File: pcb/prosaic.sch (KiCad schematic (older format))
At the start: 16 parts, among them J1 USB_C_Receptacle, SW1 SW_PUSH, U1 ATMEGA32U4, X1 XTAL_GND

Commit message: Made moutning hole rearrangements
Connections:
- net col16: now reaches U1.36 (PF7)
- net col15: now reaches U1.37 (PF6)
- no-connect marks 18 -> 16
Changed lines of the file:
@@
 Sheet 1 2
 Title "Prosaic"
-Date "2020-07-18"
-Rev "-"
+Date "2020-07-28"
+Rev "A"
 Comp ""
-Comment1 "Keyboard, Controller"
-Comment2 ""
+Comment1 "by SiriusSam"
+Comment2 "Keyboard, Controller"
 Comment3 ""
 Comment4 ""
@@
 Text Label 1500 5200 0    50   ~ 0
 col4
+Text Label 1500 5350 0    50   ~ 0
+col5
 Text Label 3400 3850 0    50   ~ 0
-col5
+col6
 Text Label 3400 4000 0    50   ~ 0
-col6
+col7
 Text Label 3400 4150 0    50   ~ 0
-col7
+col8
 Text Label 3400 4300 0    50   ~ 0
-col8
+col9
 Text Label 3400 4450 0    50   ~ 0
-col9
+col10
 Text Label 3400 4600 0    50   ~ 0
-col10
+col11
 Text Label 3400 4750 0    50   ~ 0
-col11
+col12
 Text Label 3400 4900 0    50   ~ 0
-col12
+col13
 Text Label 3400 5050 0    50   ~ 0
-col13
-Text Label 3400 5200 0    50   ~ 0
 col14
 Wire Wire Line
@@
 	1500 5200 1750 5200
 Wire Wire Line
-	3250 3850 3400 3850
-Wire Wire Line
-	3400 4000 3250 4000
-Wire Wire Line
-	3250 4150 3400 4150
-Wire Wire Line
-	3400 4300 3250 4300
+	3400 3850 3250 3850
+Wire Wire Line
+	3250 4000 3400 4000
+Wire Wire Line
+	3400 4150 3250 4150
+Wire Wire Line
+	3250 4300 3400 4300
 Wire Wire Line
 	3250 4450 3400 4450
 Wire Wire Line
-	3250 4600 3400 4600
-Wire Wire Line
-	3400 4750 3250 4750
-Wire Wire Line
-	3250 4900 3400 4900
-Wire Wire Line
-	3400 5050 3250 5050
-Wire Wire Line
-	3250 5200 3400 5200
+	3400 4600 3250 4600
+Wire Wire Line
+	3250 4750 3400 4750
+Wire Wire Line
+	3400 4900 3250 4900
+Wire Wire Line
+	3250 5050 3400 5050
 Text Label 6400 4250 0    50   ~ 0
 row0
@@
 	8900 5450 8800 5450
 NoConn ~ 8800 3750
-NoConn ~ 8800 4250
-NoConn ~ 8800 4350
 NoConn ~ 8800 4750
 NoConn ~ 8800 4850
@@
 NoConn ~ 5500 3700
 $Sheet
-S 1750 3750 1500 1550
+S 1750 3750 1500 1700
 U 5F1B28AF
 F0 "Switch Matrix" 50
@@
 F10 "col3" I L 1750 5050 50
 F11 "col4" I L 1750 5200 50
-F12 "col5" I R 3250 3850 50
-F13 "col6" I R 3250 4000 50
-F14 "col7" I R 3250 4150 50
-F15 "col8" I R 3250 4300 50
-F16 "col9" I R 3250 4450 50
-F17 "col10" I R 3250 4600 50
-F18 "col11" I R 3250 4750 50
-F19 "col12" I R 3250 4900 50
-F20 "col13" I R 3250 5050 50
-F21 "col14" I R 3250 5200 50
+F12 "col5" I L 1750 5350 50
+F13 "col6" I R 3250 3850 50
+F14 "col7" I R 3250 4000 50
+F15 "col8" I R 3250 4150 50
+F16 "col9" I R 3250 4300 50
+F17 "col10" I R 3250 4450 50
+F18 "col11" I R 3250 4600 50
+F19 "col12" I R 3250 4750 50
+F20 "col13" I R 3250 4900 50
+F21 "col14" I R 3250 5050 50
+F22 "col15" I R 3250 5200 50
+F23 "col16" I R 3250 5350 50
 $EndSheet
+Wire Wire Line
+	1500 5350 1750 5350
+Text Label 3400 5200 0    50   ~ 0
+col15
+Text Label 3400 5350 0    50   ~ 0
+col16
+Wire Wire Line
+	3250 5200 3400 5200
+Wire Wire Line
+	3250 5350 3400 5350
+Text Label 8900 4250 0    50   ~ 0
+col15
+Text Label 8900 4350 0    50   ~ 0
+col16
+Wire Wire Line
+	8800 4250 8900 4250
+Wire Wire Line
+	8800 4350 8900 4350
 $EndSCHEMATC

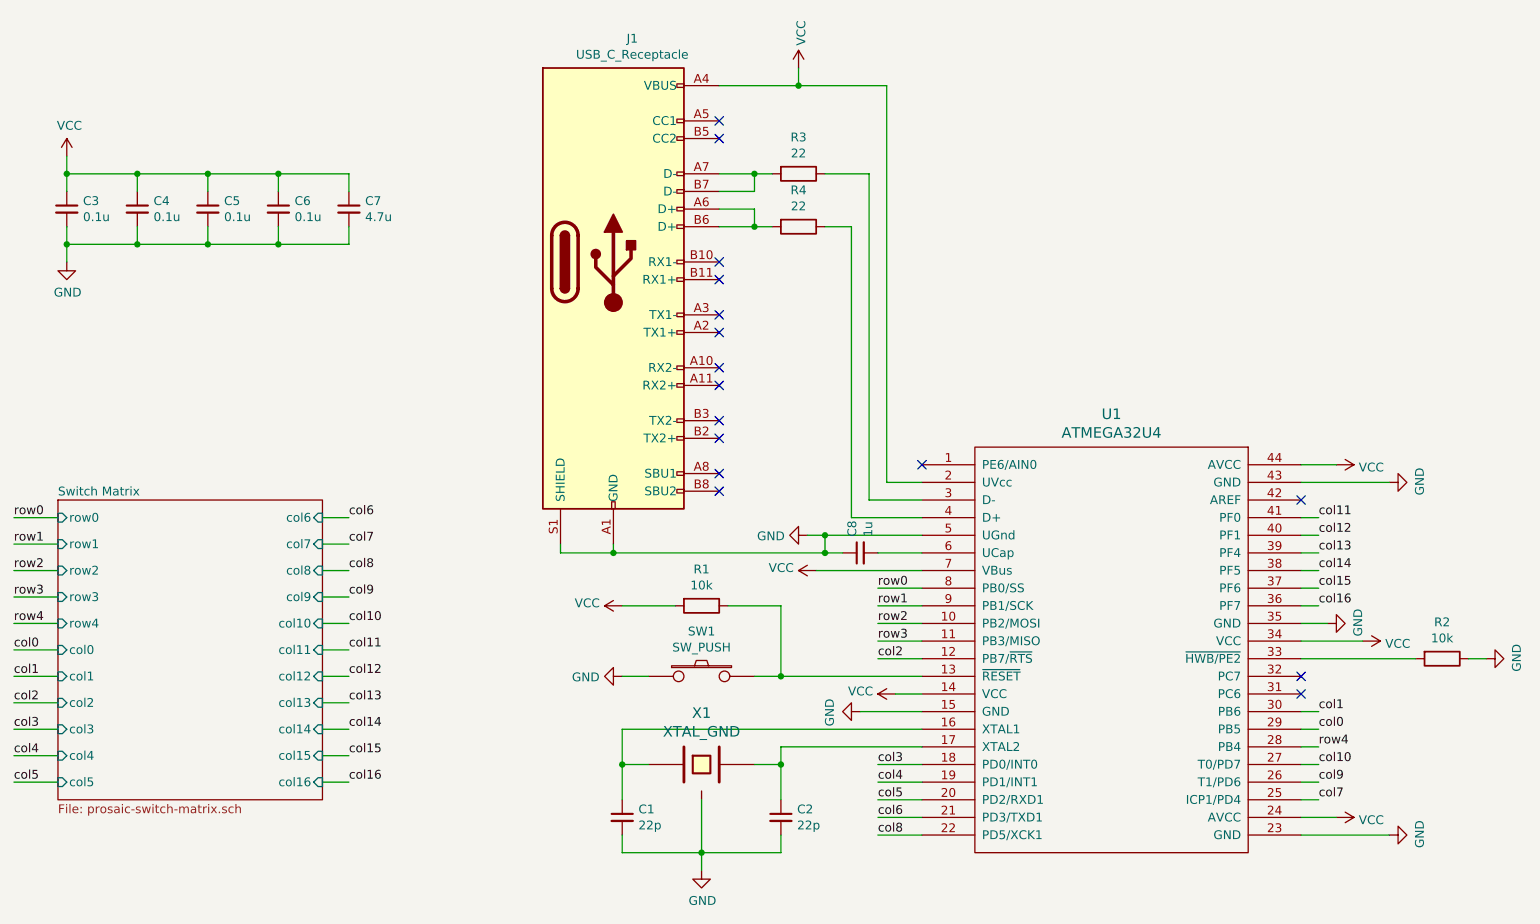
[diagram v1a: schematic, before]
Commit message: WIP: Ready for stabilizer verification
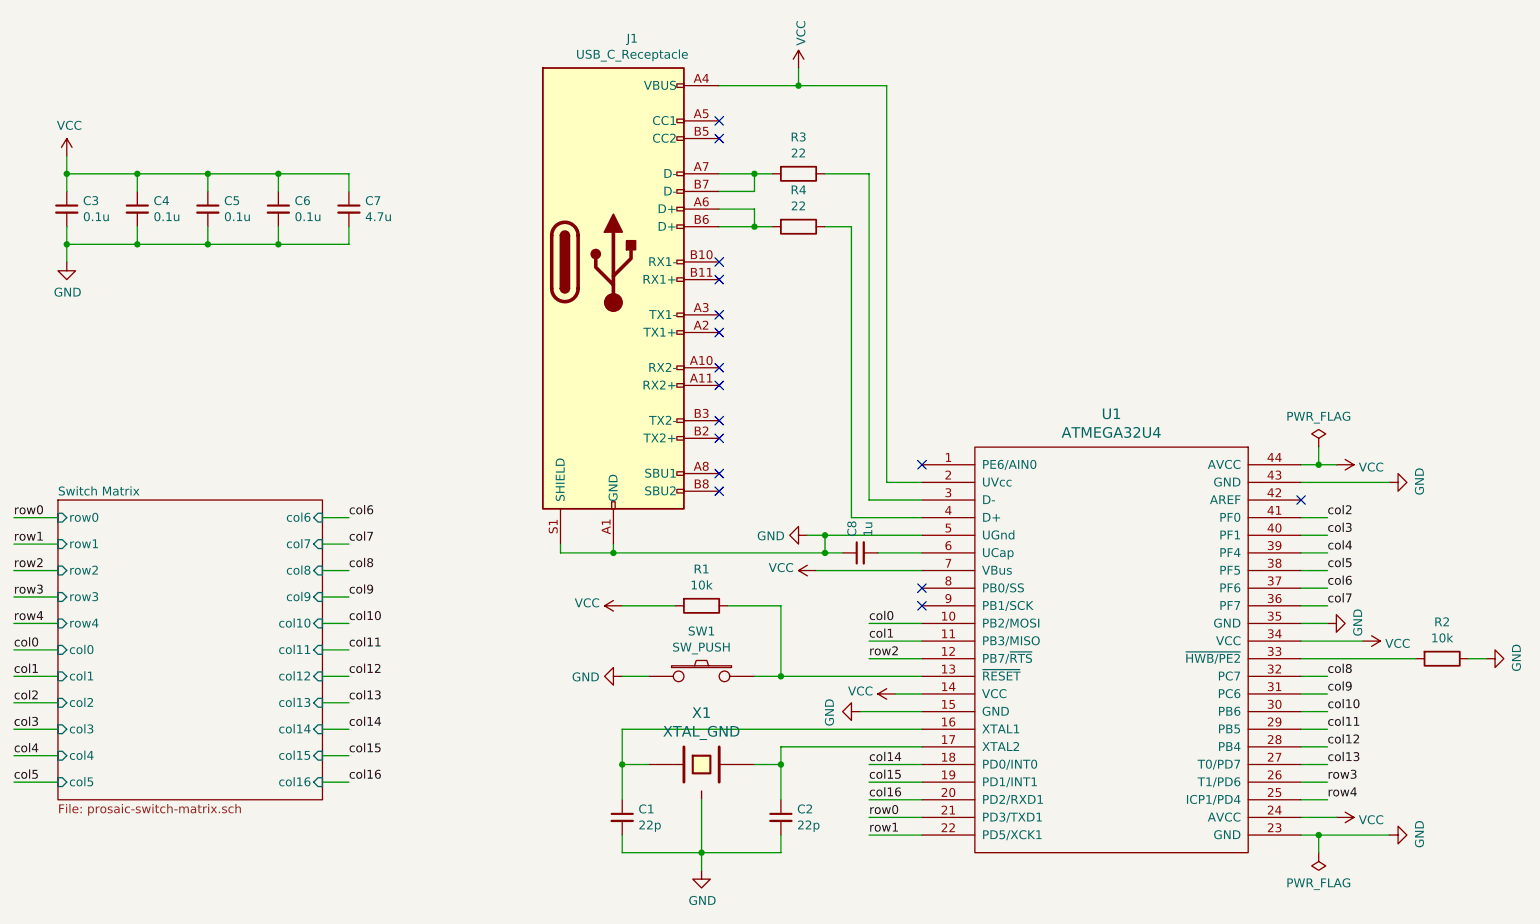
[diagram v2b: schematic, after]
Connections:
- net col0: now also U1.10 (PB2/MOSI); no longer U1.29 (PB5)
- net col1: now also U1.11 (PB3/MISO); no longer U1.30 (PB6)
- net col10: now also U1.30 (PB6); no longer U1.27 (T0/PD7)
- net col11: now also U1.29 (PB5); no longer U1.41 (PF0)
- net col12: now also U1.28 (PB4); no longer U1.40 (PF1)
- net col13: now also U1.27 (T0/PD7); no longer U1.39 (PF4)
- net col14: now also U1.18 (PD0/INT0); no longer U1.38 (PF5)
- net col15: now also U1.19 (PD1/INT1); no longer U1.37 (PF6)
- net col16: now also U1.20 (PD2/RXD1); no longer U1.36 (PF7)
- net col2: now also U1.41 (PF0); no longer U1.12 (PB7/~RTS)
- net col3: now also U1.40 (PF1); no longer U1.18 (PD0/INT0)
- net col4: now also U1.39 (PF4); no longer U1.19 (PD1/INT1)
- net col5: now also U1.38 (PF5); no longer U1.20 (PD2/RXD1)
- net col6: now also U1.37 (PF6); no longer U1.21 (PD3/TXD1)
- net col7: now also U1.36 (PF7); no longer U1.25 (ICP1/PD4)
- net col8: now also U1.32 (PC7); no longer U1.22 (PD5/XCK1)
- net col9: now also U1.31 (PC6); no longer U1.26 (T1/PD6)
- net row0: now also U1.21 (PD3/TXD1); no longer U1.8 (PB0/SS)
- net row1: now also U1.22 (PD5/XCK1); no longer U1.9 (PB1/SCK)
- net row2: now also U1.12 (PB7/~RTS); no longer U1.10 (PB2/MOSI)
- net row3: now also U1.26 (T1/PD6); no longer U1.11 (PB3/MISO)
- net row4: now also U1.25 (ICP1/PD4); no longer U1.28 (PB4)
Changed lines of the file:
@@
 Comment4 ""
 $EndDescr
-Wire Wire Line
-	6300 4950 6650 4950
 $Comp
 L power:GND #PWR0101
@@
 	0    1    1    0
 $EndComp
-Wire Wire Line
-	6500 4850 6650 4850
 $Comp
 L power:VCC #PWR0102
@@
 	0    -1   -1   0
 $EndComp
-Wire Wire Line
-	9000 5550 8800 5550
-Wire Wire Line
-	8800 5650 9300 5650
 $Comp
 L power:GND #PWR0104
@@
 	0    1    1    0
 $EndComp
-Wire Wire Line
-	8950 4450 8800 4450
 $Comp
 L power:GND #PWR0107
@@
 Wire Wire Line
 	8800 3650 9300 3650
-Wire Wire Line
-	8800 3550 9000 3550
 $Comp
 L power:GND #PWR0108
@@
 $EndComp
 Connection ~ 6100 4050
-Connection ~ 4900 4050
-Wire Wire Line
-	4900 4050 6100 4050
-Wire Wire Line
-	4600 4050 4900 4050
 Wire Wire Line
 	6100 3950 6650 3950
@@
 Text Label 1500 4750 0    50   ~ 0
 col1
-Text Label 1500 4900 0    50   ~ 0
-col2
 Text Label 1500 5050 0    50   ~ 0
 col3
@@
 	1750 4750 1500 4750
 Wire Wire Line
-	1500 4900 1750 4900
-Wire Wire Line
 	1750 5050 1500 5050
 Wire Wire Line
@@
 Wire Wire Line
 	3250 5050 3400 5050
-Text Label 6400 4250 0    50   ~ 0
-row0
-Text Label 6400 4350 0    50   ~ 0
-row1
-Text Label 6400 4450 0    50   ~ 0
-row2
-Text Label 6400 4550 0    50   ~ 0
-row3
-Text Label 8900 5150 0    50   ~ 0
-row4
-Text Label 8900 5050 0    50   ~ 0
-col0
-Text Label 8900 4950 0    50   ~ 0
-col1
-Text Label 6400 4650 0    50   ~ 0
-col2
-Text Label 6400 5250 0    50   ~ 0
-col3
-Text Label 6400 5350 0    50   ~ 0
-col4
-Text Label 6400 5450 0    50   ~ 0
-col5
-Text Label 6400 5550 0    50   ~ 0
-col6
-Text Label 8900 5450 0    50   ~ 0
-col7
-Text Label 6400 5650 0    50   ~ 0
-col8
-Text Label 8900 5350 0    50   ~ 0
-col9
-Text Label 8900 5250 0    50   ~ 0
-col10
-Text Label 8900 3850 0    50   ~ 0
-col11
-Text Label 8900 3950 0    50   ~ 0
-col12
-Text Label 8900 4050 0    50   ~ 0
-col13
-Text Label 8900 4150 0    50   ~ 0
-col14
-Wire Wire Line
-	6400 4250 6650 4250
-Wire Wire Line
-	6400 4350 6650 4350
-Wire Wire Line
-	6400 4450 6650 4450
-Wire Wire Line
-	6400 4550 6650 4550
-Wire Wire Line
-	6400 4650 6650 4650
-Wire Wire Line
-	6400 5250 6650 5250
-Wire Wire Line
-	6400 5350 6650 5350
-Wire Wire Line
-	6650 5450 6400 5450
-Wire Wire Line
-	6400 5550 6650 5550
-Wire Wire Line
-	6650 5650 6400 5650
-Wire Wire Line
-	8800 3850 8900 3850
-Wire Wire Line
-	8900 3950 8800 3950
-Wire Wire Line
-	8800 4050 8900 4050
-Wire Wire Line
-	8900 4150 8800 4150
-Wire Wire Line
-	8800 4950 8900 4950
-Wire Wire Line
-	8900 5050 8800 5050
-Wire Wire Line
-	8800 5150 8900 5150
-Wire Wire Line
-	8900 5250 8800 5250
-Wire Wire Line
-	8800 5350 8900 5350
-Wire Wire Line
-	8900 5450 8800 5450
 NoConn ~ 8800 3750
-NoConn ~ 8800 4750
-NoConn ~ 8800 4850
-NoConn ~ 6650 3550
 Wire Wire Line
 	6100 1900 6350 1900
@@
 Wire Wire Line
 	5950 1400 5500 1400
-Wire Wire Line
-	4900 4050 4900 4000
 $Comp
 L Connector:USB_C_Receptacle J1
@@
 F7 "col0" I L 1750 4600 50
 F8 "col1" I L 1750 4750 50
-F9 "col2" I L 1750 4900 50
-F10 "col3" I L 1750 5050 50
-F11 "col4" I L 1750 5200 50
-F12 "col5" I L 1750 5350 50
-F13 "col6" I R 3250 3850 50
-F14 "col7" I R 3250 4000 50
-F15 "col8" I R 3250 4150 50
-F16 "col9" I R 3250 4300 50
-F17 "col10" I R 3250 4450 50
-F18 "col11" I R 3250 4600 50
-F19 "col12" I R 3250 4750 50
-F20 "col13" I R 3250 4900 50
-F21 "col14" I R 3250 5050 50
-F22 "col15" I R 3250 5200 50
-F23 "col16" I R 3250 5350 50
+F9 "col3" I L 1750 5050 50
+F10 "col4" I L 1750 5200 50
+F11 "col5" I L 1750 5350 50
+F12 "col6" I R 3250 3850 50
+F13 "col7" I R 3250 4000 50
+F14 "col8" I R 3250 4150 50
+F15 "col9" I R 3250 4300 50
+F16 "col10" I R 3250 4450 50
+F17 "col11" I R 3250 4600 50
+F18 "col12" I R 3250 4750 50
+F19 "col13" I R 3250 4900 50
+F20 "col14" I R 3250 5050 50
+F21 "col15" I R 3250 5200 50
+F22 "col16" I R 3250 5350 50
+F23 "col2" I L 1750 4900 50
 $EndSheet
 Wire Wire Line
@@
 Wire Wire Line
 	3250 5350 3400 5350
-Text Label 8900 4250 0    50   ~ 0
+Text Label 6350 5250 0    50   ~ 0
+col14
+Text Label 6350 5350 0    50   ~ 0
 col15
-Text Label 8900 4350 0    50   ~ 0
+Text Label 6350 5450 0    50   ~ 0
 col16
-Wire Wire Line
-	8800 4250 8900 4250
-Wire Wire Line
-	8800 4350 8900 4350
+Text Label 6350 5550 0    50   ~ 0
+row0
+Text Label 6350 5650 0    50   ~ 0
+row1
+Wire Wire Line
+	6350 5250 6650 5250
+Wire Wire Line
+	6650 5350 6350 5350
+Wire Wire Line
+	6350 5450 6650 5450
+Wire Wire Line
+	6650 5550 6350 5550
+Wire Wire Line
+	6350 5650 6650 5650
+Text Label 8950 5450 0    50   ~ 0
+row4
+Text Label 8950 5350 0    50   ~ 0
+row3
+Text Label 6350 4650 0    50   ~ 0
+row2
+Text Label 8950 5250 0    50   ~ 0
+col13
+Text Label 8950 5150 0    50   ~ 0
+col12
+Text Label 8950 5050 0    50   ~ 0
+col11
+Text Label 8950 4950 0    50   ~ 0
+col10
+Text Label 8950 4850 0    50   ~ 0
+col9
+Text Label 8950 4750 0    50   ~ 0
+col8
+Text Label 8950 4350 0    50   ~ 0
+col7
+Text Label 8950 4250 0    50   ~ 0
+col6
+Text Label 8950 4150 0    50   ~ 0
+col5
+Text Label 8950 4050 0    50   ~ 0
+col4
+Text Label 8950 3950 0    50   ~ 0
+col3
+Text Label 6350 4550 0    50   ~ 0
+col1
+Text Label 6350 4450 0    50   ~ 0
+col0
+Wire Wire Line
+	6350 4450 6650 4450
+Wire Wire Line
+	6650 4550 6350 4550
+Wire Wire Line
+	6350 4650 6650 4650
+Wire Wire Line
+	8800 5450 8950 5450
+Wire Wire Line
+	8950 5350 8800 5350
+Wire Wire Line
+	8800 5250 8950 5250
+Wire Wire Line
+	8950 5150 8800 5150
+Wire Wire Line
+	8800 5050 8950 5050
+Wire Wire Line
+	8950 4950 8800 4950
+Wire Wire Line
+	8800 4850 8950 4850
+Wire Wire Line
+	8950 4750 8800 4750
+Wire Wire Line
+	8800 3950 8950 3950
+Wire Wire Line
+	8950 4050 8800 4050
+Wire Wire Line
+	8800 4150 8950 4150
+Wire Wire Line
+	8950 4250 8800 4250
+Wire Wire Line
+	8800 4350 8950 4350
+NoConn ~ 6650 4250
+NoConn ~ 6650 4350
+NoConn ~ 6650 3550
+Wire Wire Line
+	8800 3550 8900 3550
+Wire Wire Line
+	8800 5550 9000 5550
+Wire Wire Line
+	4600 4050 4900 4050
+Wire Wire Line
+	4900 4000 4900 4050
+Connection ~ 4900 4050
+Wire Wire Line
+	4900 4050 6100 4050
+Text Label 1500 4900 0    50   ~ 0
+col2
+Wire Wire Line
+	1500 4900 1750 4900
+Text Label 8950 3850 0    50   ~ 0
+col2
+Wire Wire Line
+	8950 3850 8800 3850
+Wire Wire Line
+	8800 4450 8950 4450
+Wire Wire Line
+	6300 4950 6650 4950
+Wire Wire Line
+	6500 4850 6650 4850
+Wire Wire Line
+	8800 5650 8900 5650
+$Comp
+L power:PWR_FLAG #FLG0101
+U 1 1 5F3379B5
+P 8900 3450
+F 0 "#FLG0101" H 8900 3525 50  0001 C CNN
+F 1 "PWR_FLAG" H 8900 3623 50  0000 C CNN
+F 2 "" H 8900 3450 50  0001 C CNN
+F 3 "~" H 8900 3450 50  0001 C CNN
+	1    8900 3450
+	1    0    0    -1
+$EndComp
+Wire Wire Line
+	8900 3450 8900 3550
+Connection ~ 8900 3550
+Wire Wire Line
+	8900 3550 9000 3550
+$Comp
+L power:PWR_FLAG #FLG0102
+U 1 1 5F344283
+P 8900 5750
+F 0 "#FLG0102" H 8900 5825 50  0001 C CNN
+F 1 "PWR_FLAG" H 8900 5923 50  0000 C CNN
+F 2 "" H 8900 5750 50  0001 C CNN
+F 3 "~" H 8900 5750 50  0001 C CNN
+	1    8900 5750
+	-1   0    0    1
+$EndComp
+Wire Wire Line
+	8900 5750 8900 5650
+Connection ~ 8900 5650
+Wire Wire Line
+	8900 5650 9300 5650
 $EndSCHEMATC

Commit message: Completed revision with new PCB layout
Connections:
- net col1: now also U1.9 (PB1/SCK); no longer U1.11 (PB3/MISO)
- net col10: now also U1.40 (PF1); no longer U1.30 (PB6)
- net col11: now also U1.28 (PB4); no longer U1.29 (PB5)
- net col12: now also U1.27 (T0/PD7); no longer U1.28 (PB4)
- net col13: now also U1.12 (PB7/~RTS); no longer U1.27 (T0/PD7)
- net col2: now also U1.29 (PB5); no longer U1.41 (PF0)
- net col3: now also U1.30 (PB6); no longer U1.40 (PF1)
- net col4: now also U1.31 (PC6); no longer U1.39 (PF4)
- net col5: now also U1.32 (PC7); no longer U1.38 (PF5)
- net col6: now also U1.36 (PF7); no longer U1.37 (PF6)
- net col7: now also U1.37 (PF6); no longer U1.36 (PF7)
- net col8: now also U1.38 (PF5); no longer U1.32 (PC7)
- net col9: now also U1.39 (PF4); no longer U1.31 (PC6)
- net row2: now also U1.11 (PB3/MISO); no longer U1.12 (PB7/~RTS)
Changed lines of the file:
@@
 Text Label 8950 5350 0    50   ~ 0
 row3
+Text Label 6350 4550 0    50   ~ 0
+row2
 Text Label 6350 4650 0    50   ~ 0
-row2
+col13
 Text Label 8950 5250 0    50   ~ 0
-col13
+col12
 Text Label 8950 5150 0    50   ~ 0
-col12
-Text Label 8950 5050 0    50   ~ 0
 col11
+Text Label 8950 3950 0    50   ~ 0
+col10
+Text Label 8950 4050 0    50   ~ 0
+col9
+Text Label 8950 4150 0    50   ~ 0
+col8
+Text Label 8950 4250 0    50   ~ 0
+col7
+Text Label 8950 4350 0    50   ~ 0
+col6
+Text Label 8950 4750 0    50   ~ 0
+col5
+Text Label 8950 4850 0    50   ~ 0
+col4
 Text Label 8950 4950 0    50   ~ 0
-col10
-Text Label 8950 4850 0    50   ~ 0
-col9
-Text Label 8950 4750 0    50   ~ 0
-col8
-Text Label 8950 4350 0    50   ~ 0
-col7
-Text Label 8950 4250 0    50   ~ 0
-col6
-Text Label 8950 4150 0    50   ~ 0
-col5
-Text Label 8950 4050 0    50   ~ 0
-col4
-Text Label 8950 3950 0    50   ~ 0
 col3
-Text Label 6350 4550 0    50   ~ 0
+Text Label 6350 4350 0    50   ~ 0
 col1
 Text Label 6350 4450 0    50   ~ 0
 col0
 Wire Wire Line
-	6350 4450 6650 4450
+	6350 4350 6650 4350
 Wire Wire Line
-	6650 4550 6350 4550
+	6650 4450 6350 4450
 Wire Wire Line
-	6350 4650 6650 4650
+	6350 4550 6650 4550
 Wire Wire Line
 	8800 5450 8950 5450
@@
 	8800 4350 8950 4350
 NoConn ~ 6650 4250
-NoConn ~ 6650 4350
 NoConn ~ 6650 3550
 Wire Wire Line
@@
 Wire Wire Line
 	1500 4900 1750 4900
-Text Label 8950 3850 0    50   ~ 0
+Text Label 8950 5050 0    50   ~ 0
 col2
 Wire Wire Line
@@
 Wire Wire Line
 	8900 5650 9300 5650
+NoConn ~ 8950 3850
+Wire Wire Line
+	6350 4650 6650 4650
 $EndSCHEMATC
